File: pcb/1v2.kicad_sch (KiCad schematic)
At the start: 3 parts, among them U4 TLV74312PDBVR

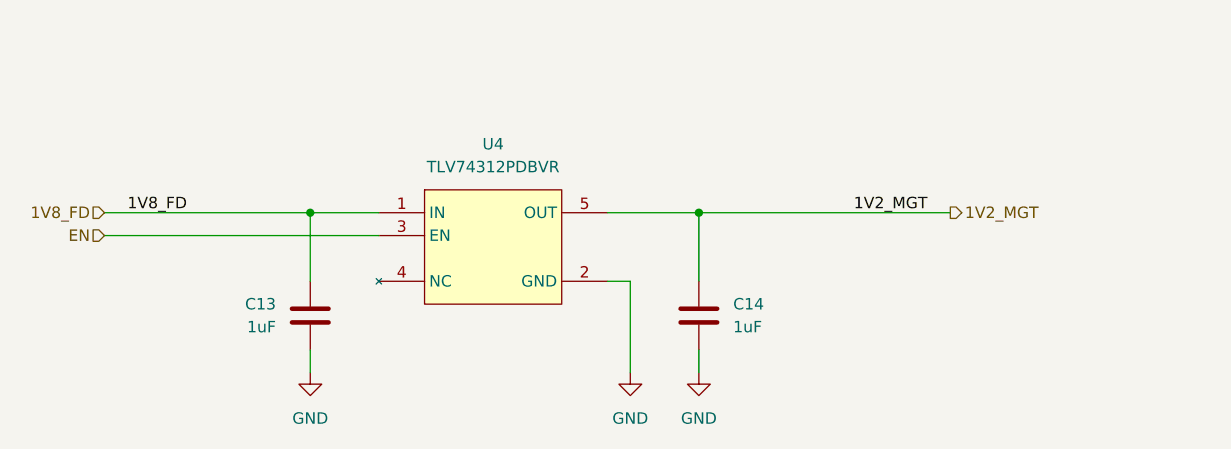
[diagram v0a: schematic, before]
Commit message: changes to power tree
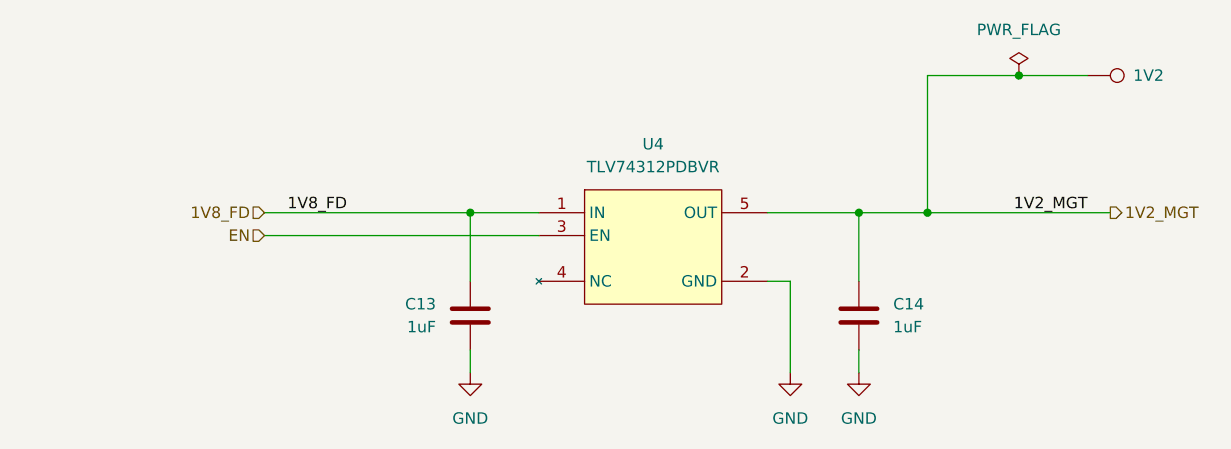
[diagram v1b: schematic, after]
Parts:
- added 1V2: TestPoint, TestPoint:TestPoint_Pad_D1.0mm, symbol library:TestPoint
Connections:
- net 1V2_MGT: now also 1V2.1
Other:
- moved on the sheet: C13, C14, U4

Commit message: moved stuff around, bom
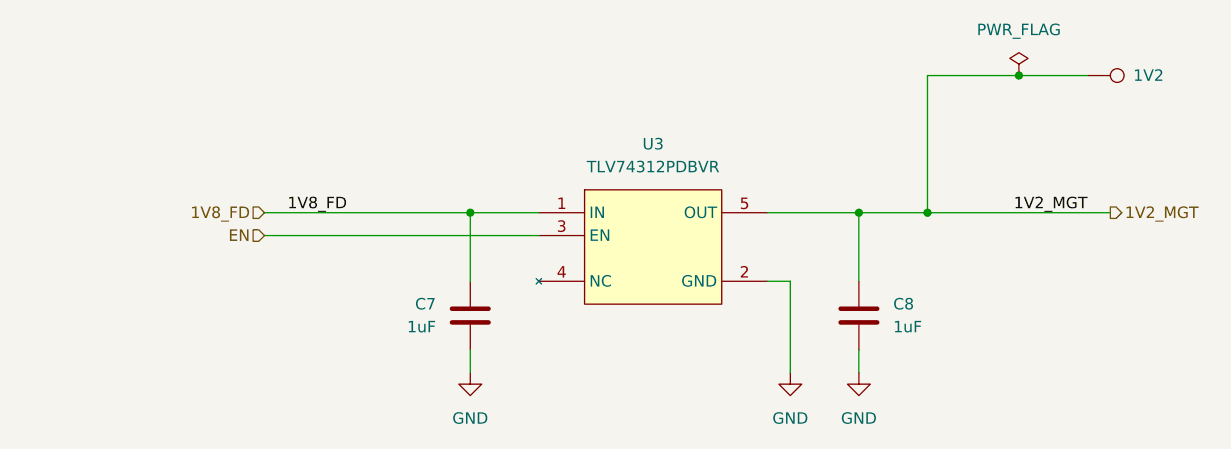
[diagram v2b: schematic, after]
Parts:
- renumbered C13 to C7, C14 to C8, U4 to U3
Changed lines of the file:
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@@
 		(at 127 88.9)
 		(diameter 0)
-		(color 0 0 0 0)
+		(color 255 0 0 1)
 	)
 	(junction
@@
 		(on_board yes)
 		(dnp no)
-		(property "Reference" "#PWR017"
+		(property "Reference" "#PWR010"
 			(at 162.56 113.03 0)
 			(effects
@@
 			(project "RPi-HwAB-1"
 				(path "/e63e39d7-6ac0-4ffd-8aa3-1841a4541b55/f9ebb56c-78c7-42ac-bc19-ccbf788f5318/1d9f07e5-efc9-447f-a372-e965921820d7"
-					(reference "#PWR017")
+					(reference "#PWR010")
 					(unit 1)
 				)
@@
 		(dnp no)
 		(fields_autoplaced yes)
-		(property "Reference" "#PWR039"
+		(property "Reference" "#PWR011"
 			(at 170.18 113.03 0)
 			(effects
@@
 			(project "RPi-HwAB-1"
 				(path "/e63e39d7-6ac0-4ffd-8aa3-1841a4541b55/f9ebb56c-78c7-42ac-bc19-ccbf788f5318/1d9f07e5-efc9-447f-a372-e965921820d7"
-					(reference "#PWR039")
+					(reference "#PWR011")
 					(unit 1)
 				)
@@
 		(dnp no)
 		(fields_autoplaced yes)
-		(property "Reference" "#PWR06"
+		(property "Reference" "#PWR09"
 			(at 127 113.03 0)
 			(effects
@@
 			(project "RPi-HwAB-1"
 				(path "/e63e39d7-6ac0-4ffd-8aa3-1841a4541b55/f9ebb56c-78c7-42ac-bc19-ccbf788f5318/1d9f07e5-efc9-447f-a372-e965921820d7"
-					(reference "#PWR06")
+					(reference "#PWR09")
 					(unit 1)
 				)
@@
 		(dnp no)
 		(fields_autoplaced yes)
-		(property "Reference" "U4"
+		(property "Reference" "U3"
 			(at 147.32 81.28 0)
 			(effects
@@
 			(project "RPi-HwAB-1"
 				(path "/e63e39d7-6ac0-4ffd-8aa3-1841a4541b55/f9ebb56c-78c7-42ac-bc19-ccbf788f5318/1d9f07e5-efc9-447f-a372-e965921820d7"
-					(reference "U4")
+					(reference "U3")
 					(unit 1)
 				)
@@
 		(on_board yes)
 		(dnp no)
-		(property "Reference" "C13"
+		(property "Reference" "C7"
 			(at 123.19 99.0599 0)
 			(effects
@@
 			(project "RPi-HwAB-1"
 				(path "/e63e39d7-6ac0-4ffd-8aa3-1841a4541b55/f9ebb56c-78c7-42ac-bc19-ccbf788f5318/1d9f07e5-efc9-447f-a372-e965921820d7"
-					(reference "C13")
+					(reference "C7")
 					(unit 1)
 				)
@@
 		(on_board yes)
 		(dnp no)
-		(property "Reference" "C14"
+		(property "Reference" "C8"
 			(at 173.99 99.0599 0)
 			(effects
@@
 			(project "RPi-HwAB-1"
 				(path "/e63e39d7-6ac0-4ffd-8aa3-1841a4541b55/f9ebb56c-78c7-42ac-bc19-ccbf788f5318/1d9f07e5-efc9-447f-a372-e965921820d7"
-					(reference "C14")
+					(reference "C8")
 					(unit 1)
 				)
@@
 		(dnp no)
 		(fields_autoplaced yes)
-		(property "Reference" "#FLG03"
+		(property "Reference" "#FLG02"
 			(at 187.96 71.755 0)
 			(effects
@@
 			(project ""
 				(path "/e63e39d7-6ac0-4ffd-8aa3-1841a4541b55/f9ebb56c-78c7-42ac-bc19-ccbf788f5318/1d9f07e5-efc9-447f-a372-e965921820d7"
-					(reference "#FLG03")
+					(reference "#FLG02")
 					(unit 1)
 				)

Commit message: bom
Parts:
- 1V2: now left out of the parts list
- C7, C8: Part Description (none) -> CAP CER 1UF 6.3V X5R 0402
- U3: Part Description (none) -> IC REG LINEAR 1.2V 300MA SOT23-5
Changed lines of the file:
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@@
 		(unit 1)
 		(exclude_from_sim no)
-		(in_bom yes)
+		(in_bom no)
 		(on_board yes)
 		(dnp no)
@@
 		)
 		(property "Description" "test point"
+			(at 195.58 73.66 0)
+			(effects
+				(font
+					(size 1.27 1.27)
+				)
+				(hide yes)
+			)
+		)
+		(property "Name" ""
 			(at 195.58 73.66 0)
 			(effects
@@
 			)
 		)
+		(property "Part Description" "IC REG LINEAR 1.2V 300MA SOT23-5"
+			(at 147.32 99.06 0)
+			(effects
+				(font
+					(size 1.27 1.27)
+				)
+				(hide yes)
+			)
+		)
 		(pin "1"
 		)
@@
 			)
 		)
+		(property "Part Description" "CAP CER 1UF 6.3V X5R 0402"
+			(at 127 100.33 0)
+			(effects
+				(font
+					(size 1.27 1.27)
+				)
+				(hide yes)
+			)
+		)
 		(pin "1"
 		)
@@
 			(at 170.18 100.33 0)
 			(effects
+				(font
+					(size 1.27 1.27)
+				)
+				(hide yes)
+			)
+		)
+		(property "Part Description" "CAP CER 1UF 6.3V X5R 0402"
+			(at 170.18 100.33 0)
+			(effects
